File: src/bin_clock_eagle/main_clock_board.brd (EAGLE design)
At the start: 79 parts, among them IC1 DS3231/SO, Q2 16mhz, U1 ATMEGA328P-AU

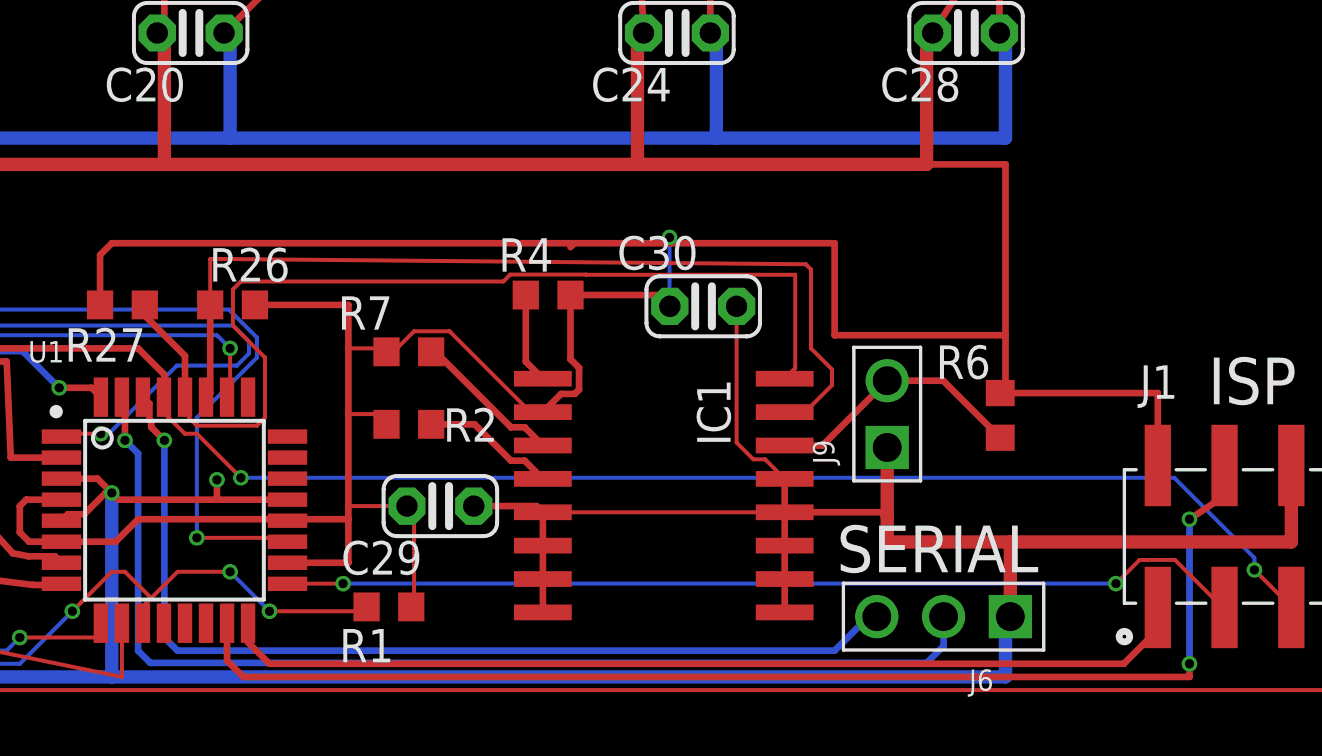
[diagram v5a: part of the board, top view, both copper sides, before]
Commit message: fixing r4,r7
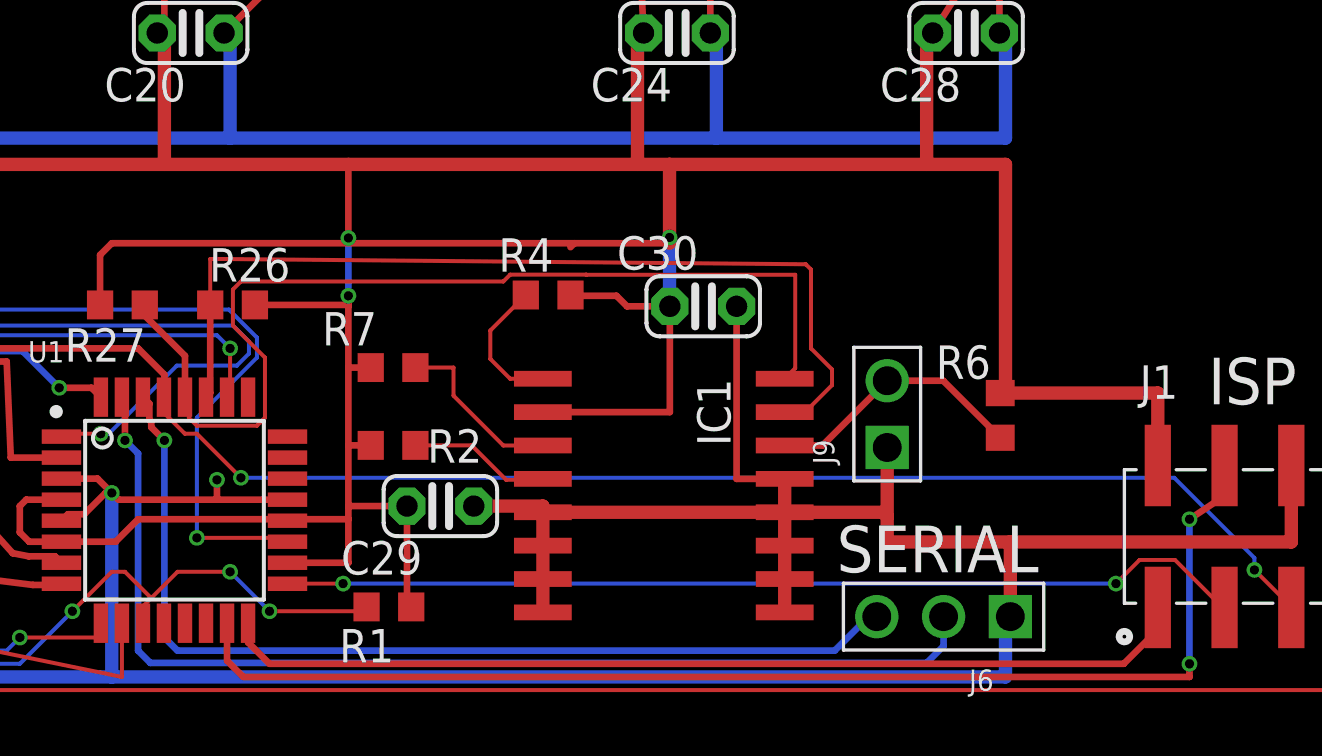
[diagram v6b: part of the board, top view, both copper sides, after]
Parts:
- moved R2 1.00 mm to (63.7, 9.31)
- moved R7 0.85 mm to (63.7, 12.3)
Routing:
- net VCC: track 728.1 -> 719.1 mm, vias 1 -> 3
- net N$43: track 3.45 -> 5.30 mm
- net N$45: track 5.73 -> 6.70 mm
- net GND: track 777.7 -> 778.7 mm
